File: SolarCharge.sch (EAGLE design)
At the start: 8 parts

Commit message: Improve GND
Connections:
- net N$2 renamed GND
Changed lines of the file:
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@@
 <?xml version="1.0" encoding="utf-8"?>
 <!DOCTYPE eagle SYSTEM "eagle.dtd">
-<eagle version="9.1.0">
+<eagle version="7.7.0">
 <drawing>
 <settings>
@@
 </segment>
 </net>
-<net name="N$2" class="0">
+<net name="GND" class="0">
 <segment>
 <pinref part="U$1" gate="G$1" pin="P$2"/>

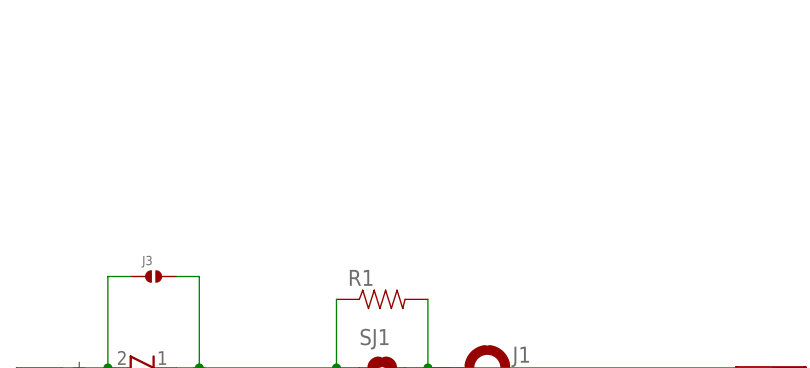
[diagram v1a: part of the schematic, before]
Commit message: Add logos, recenter
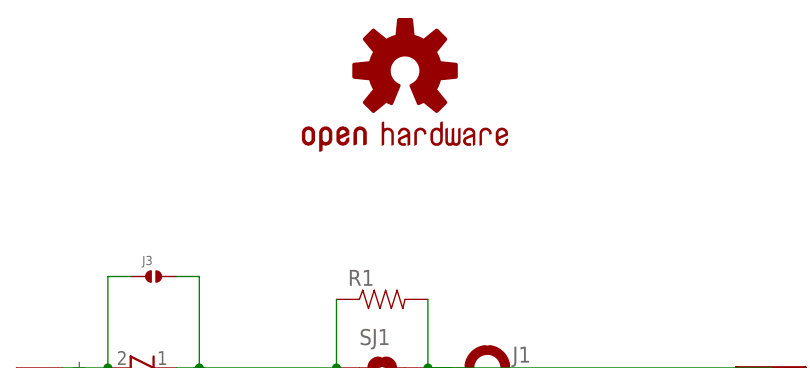
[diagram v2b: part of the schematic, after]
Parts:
- added LOGO1: OSHW-LOGOM, Spark:OSHW-LOGOM
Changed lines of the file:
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@@
 <part name="SJ1" library="SparkFun-Passives" deviceset="SOLDERJUMPER-OLD" device="TRACE"/>
 <part name="CN1" library="lio" deviceset="JST_2PIN" device="-SMT-RA"/>
+<part name="LOGO1" library="Spark" deviceset="OSHW-LOGO" device="M"/>
 </parts>
 <sheets>
@@
 <instance part="SJ1" gate="1" x="93.98" y="78.74"/>
 <instance part="CN1" gate="G$1" x="134.62" y="76.2" rot="R180"/>
+<instance part="LOGO1" gate="G$1" x="96.52" y="111.76"/>
 </instances>
 <busses>

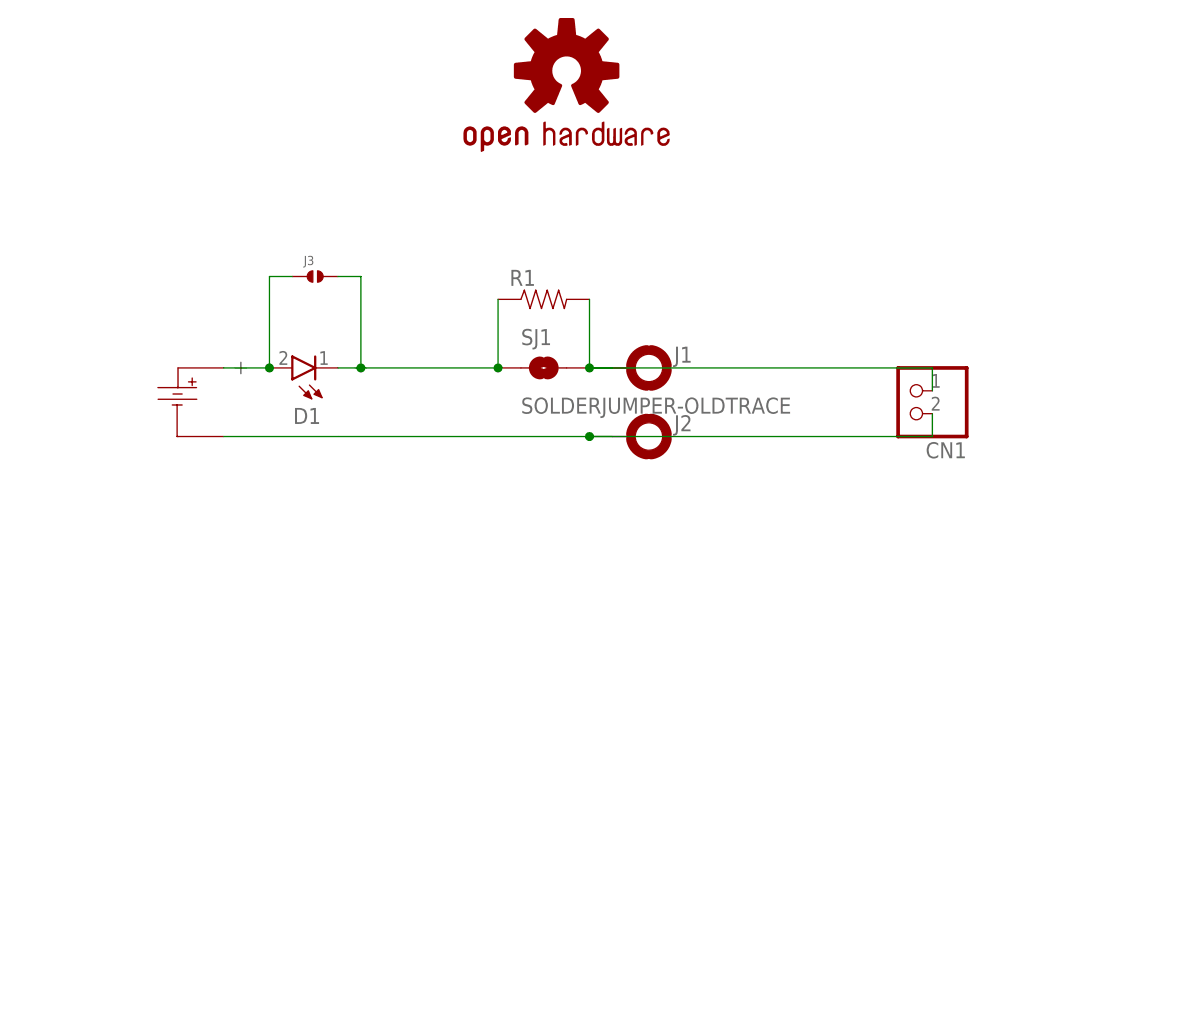
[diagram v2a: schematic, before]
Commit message: Add RGB runtime info
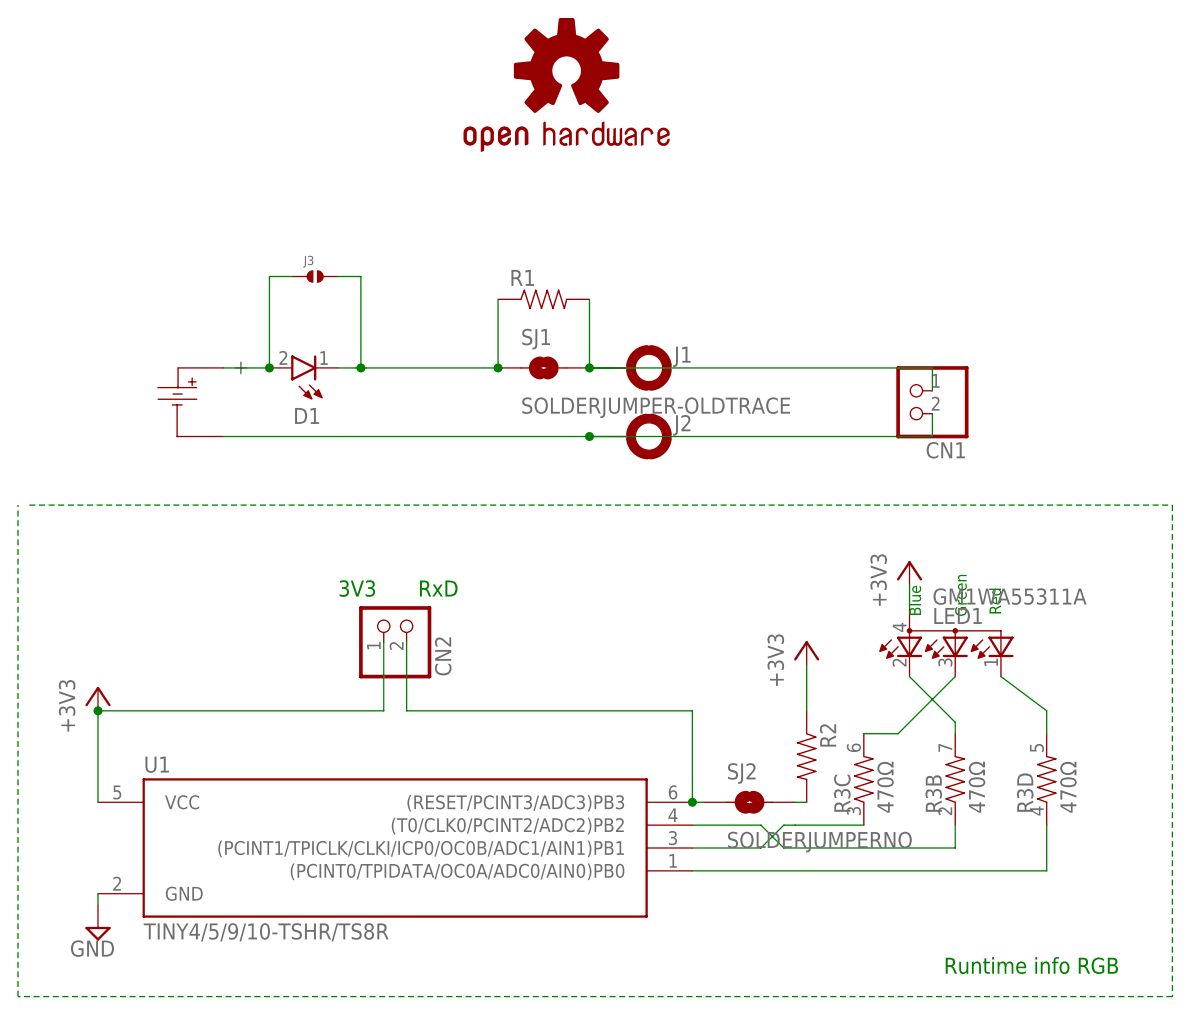
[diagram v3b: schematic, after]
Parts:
- added CN2: (no value), lio:JST_2PIN-SMT-RA
- added LED1: GM1WA55311A, led:GM1WA55311A
- added R2: (no value), ROHM:RESISTOR0603-RES
- added R3: 470Ω, SparkFun:RESISTOR-ARRAY0603-ARV
- added SJ2: SOLDERJUMPERNO, SparkFun-Passives:SOLDERJUMPERNO
- added U1: TINY4/5/9/10-TSHR/TS8R, bt_avr:TINY4/5/9/10-TSHR/TS8R
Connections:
- new net +3V3: CN2.2, LED1.A, R2.1, U1.VCC
- new net BLUE: R3C.1, U1.(PCINT1/TPICLK/CLKI/ICP0/OC0B/ADC1/AIN1)PB1
- new net GREEN: R3B.1, U1.(T0/CLK0/PCINT2/ADC2)PB2
- new net N$5: LED1.CBLUE, R3C.2
- new net N$6: LED1.CRED, R3B.2
- new net N$7: R2.2, SJ2.2
- new net RED: R3D.1, U1.(PCINT0/TPIDATA/OC0A/ADC0/AIN0)PB0
- new net RED_RESISTOR: LED1.CGREEN, R3D.2
- new net RXD: CN2.1, SJ2.1, U1.(RESET/PCINT3/ADC3)PB3
- net GND: now also U1.GND
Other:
- note added: "3V3"
- note added: "Blue"
- note added: "Green"
- note added: "Red"
- note added: "Runtime info RGB"
- note added: "RxD"
